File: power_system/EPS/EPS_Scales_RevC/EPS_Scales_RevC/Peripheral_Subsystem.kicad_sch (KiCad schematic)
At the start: 6 parts, among them J13 G125-MH11605L3P

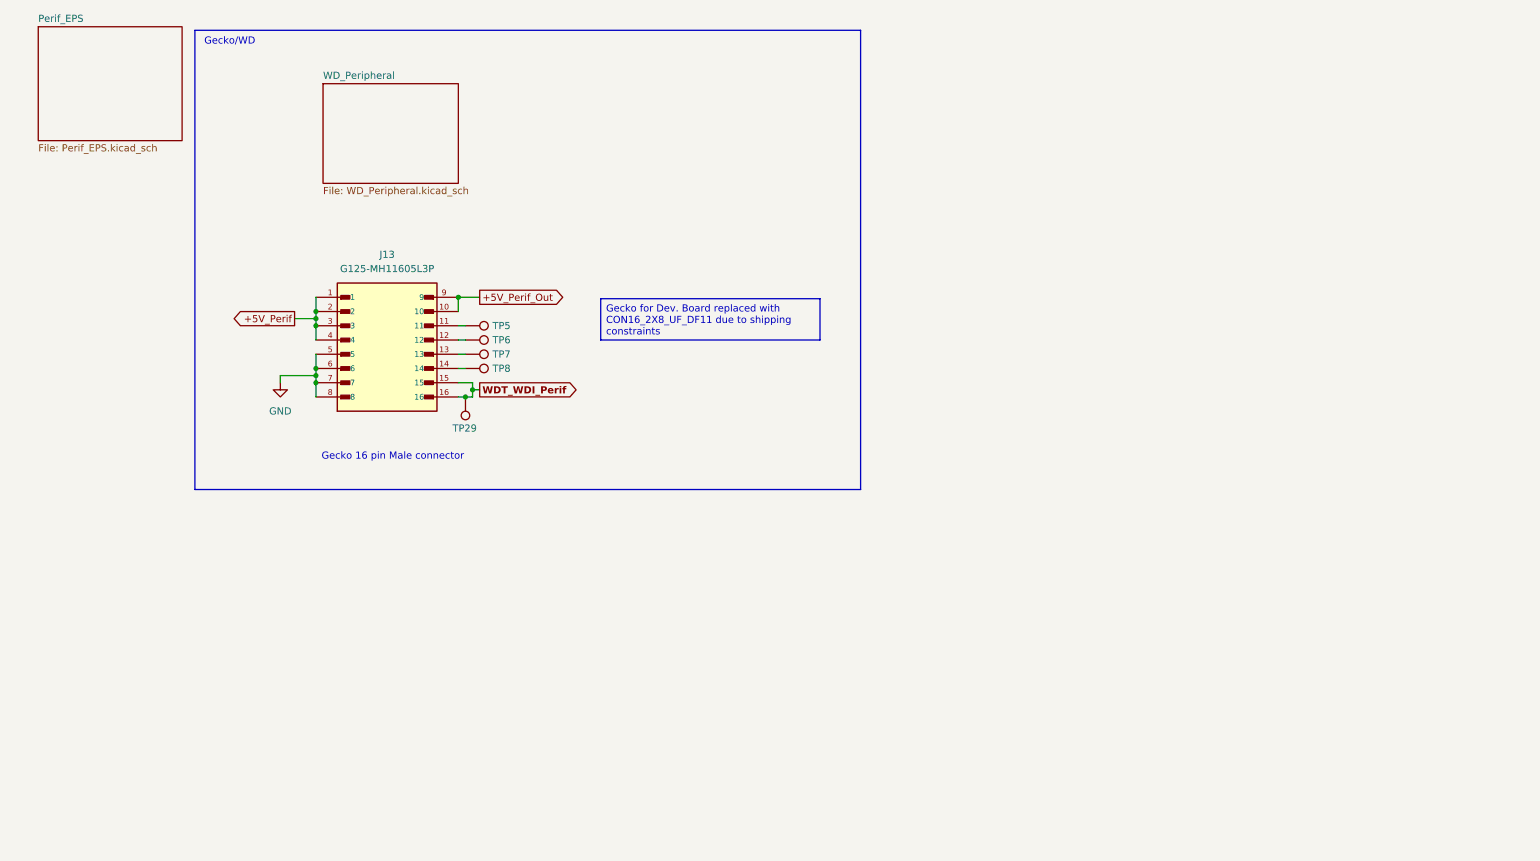
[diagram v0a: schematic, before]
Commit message: Rev C Schematic DONE
Components were finalized in meeting with Andrew Greenberg today, footprints have been assigned and specific component sizes and values have also been confirmed. Moving to layout for the first dev board of the SCALES EPS board.
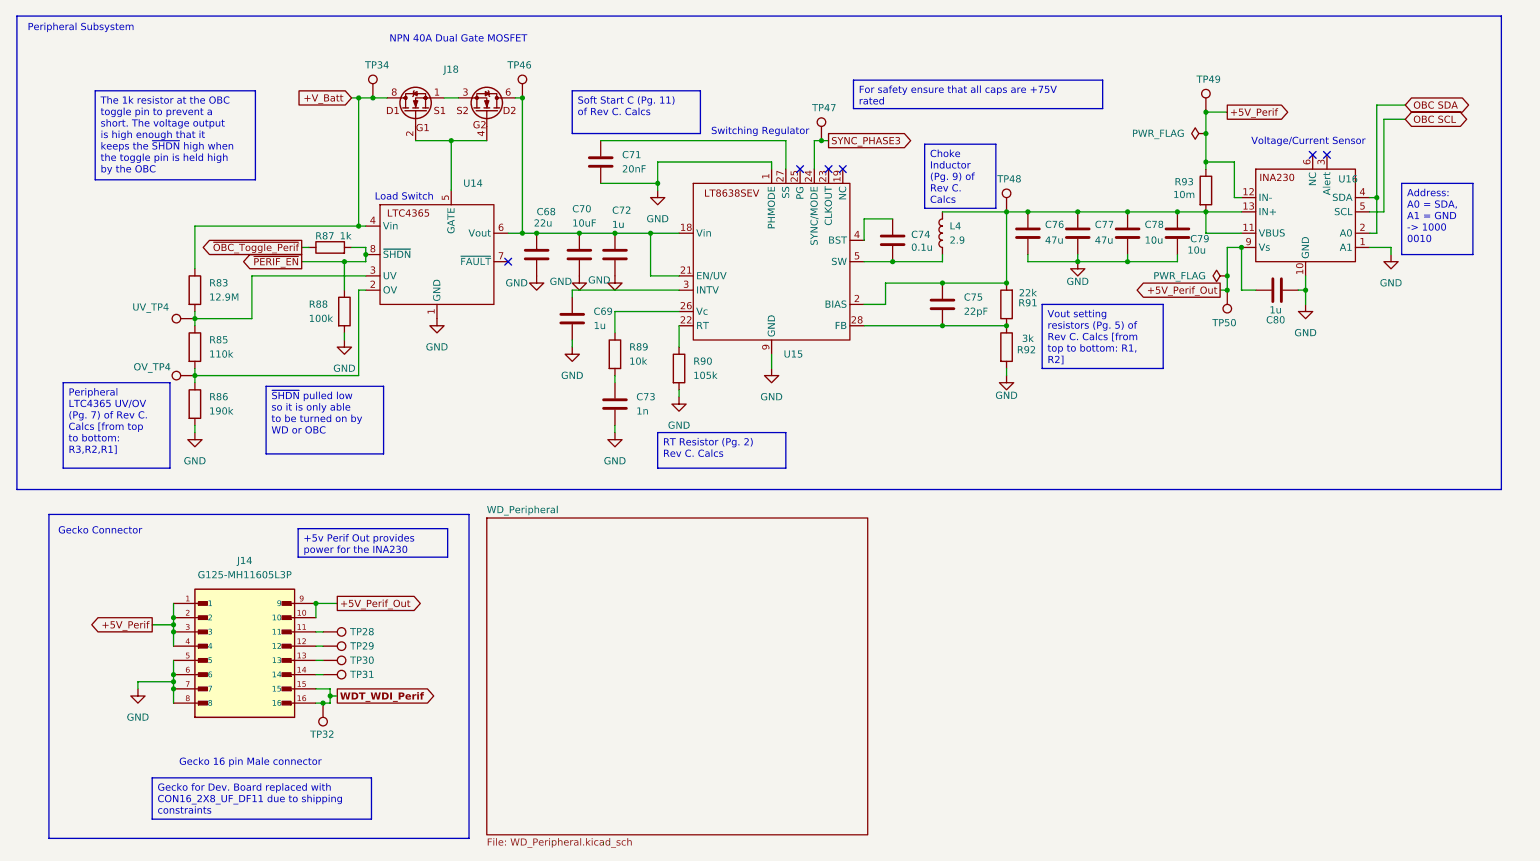
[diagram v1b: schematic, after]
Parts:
- added C68: 22u, Resistor_SMD:R_1210_3225Metric, symbol Device:C
- added C69, C72, C80: 1u, Resistor_SMD:R_1210_3225Metric, symbol Device:C
- added C70: 10uF, Resistor_SMD:R_1210_3225Metric, symbol Device:C
- added C71: 20nF, Resistor_SMD:R_1210_3225Metric, symbol Device:C
- added C73: 1n, Resistor_SMD:R_1210_3225Metric, symbol Device:C
- added C74: 0.1u, Resistor_SMD:R_1210_3225Metric, symbol Device:C
- added C75: 22pF, Resistor_SMD:R_1210_3225Metric, symbol Device:C
- added C76, C77: 47u, Resistor_SMD:R_1210_3225Metric, symbol Device:C
- added C78, C79: 10u, Resistor_SMD:R_1210_3225Metric, symbol Device:C
- added J18: ~, RevC Footprints:SISB46DN-T1-GE3, symbol SISB46DN:SISB46DN
- added L4: 2.9, RevC Footprints:XEL6030102MEC, symbol Device:L
- added OV_TP4, TP34, TP46, TP47, TP48, TP49, TP50, UV_TP4: TestPoint, TestPoint:TestPoint_Pad_1.0x1.0mm, symbol Connector:TestPoint
- added R83: 12.9M, Resistor_SMD:R_0603_1608Metric, symbol Device:R
- added R85: 110k, Resistor_SMD:R_0603_1608Metric, symbol Device:R
- added R86: 190k, Resistor_SMD:R_0603_1608Metric, symbol Device:R
- added R87: 1k, Resistor_SMD:R_0603_1608Metric, symbol Device:R
- added R88: 100k, Resistor_SMD:R_0603_1608Metric, symbol Device:R
- added R89: 10k, Resistor_SMD:R_0603_1608Metric, symbol Device:R
- added R90: 105k, Resistor_SMD:R_0603_1608Metric, symbol Device:R
- added R91: 22k, Resistor_SMD:R_0603_1608Metric, symbol Device:R
- added R92: 3k, Resistor_SMD:R_0603_1608Metric, symbol Device:R
- added R93: 10m, Resistor_SMD:R_2512_6332Metric, symbol Device:R
- added U14: ~, RevC Footprints:LTC4365, symbol LTC4365:LTC4365
- added U15: ~, RevC Footprints:LT8638SEVPBF, symbol LT8638SEV#PBF:LT863SEV#PBF
- added U16: INA230, RevC Footprints:INA230AIRGTT, symbol INA230:INA230 [RGT PACKAGE]
- renumbered J13 to J14, TP5 to TP28, TP6 to TP29, TP7 to TP30, TP8 to TP31, TP29 to TP32
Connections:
- net +5V_Perif: now also R93.1, TP49.1, U16.12 (IN-)
- net +5V_Perif_Out: now also C80.2, TP50.1, U16.9 (Vs)
- net GND: now also C68.2, C69.2, C70.2, C71.2, C72.2, C73.2, C76.2, C77.2, C78.2, C79.2, C80.1, R86.2, R88.2, R90.2, R92.2, U14.1 (GND), U15.1 (PHMODE), U15.9 (GND), U16.1 (A1), U16.10 (GND)
- new net: OV_TP4.1, R85.2, R86.1, U14.2 (OV)
- new net: J18.1, J18.3
- new net: J18.2, J18.4, U14.5 (GATE)
- new net: C68.1, C70.1, C72.1, J18.5, J18.6, TP46.1, U14.6 (Vout), U15.18 (Vin), U15.21 (EN/UV)
- new net: C75.1, C76.1, C77.1, C78.1, C79.1, L4.2, R91.2, R93.2, TP48.1, U15.2 (BIAS), U16.11 (VBUS), U16.13 (IN+)
- new net: C75.2, R91.1, R92.1, U15.28 (FB)
- new net: C71.1, U15.27 (SS)
- new net: R83.2, R85.1, U14.3 (UV), UV_TP4.1
- new net: C73.1, R89.2
- new net: R89.1, U15.26 (Vc)
- new net: C74.2, L4.1, U15.5 (SW)
- new net: R90.1, U15.22 (RT)
- new net: C69.1, U15.3 (INTV)
- new net: C74.1, U15.4 (BST)
- new net +V_Batt: J18.7, J18.8, R83.1, TP34.1, U14.4 (Vin)
- new net OBC SCL: U16.5 (SCL)
- new net OBC SDA: U16.2 (A0), U16.4 (SDA)
- new net SYNC_PHASE3: TP47.1, U15.24 (SYNC/MODE)
- new net ~{OBC_Toggle_Perif}: R87.1
- new net ~{PERIF_EN}: R87.2, R88.1, U14.8 (~{SHDN})
- no-connect marks 0 -> 6
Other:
- removed sheet Perif_EPS
- note added: "Gecko Connector"
- note added: "Load Switch"
- note added: "NPN 40A Dual Gate MOSFET"
- note added: "Peripheral Subsystem"
- note added: "Switching Regulator"
- note added: "Voltage/Current Sensor"
- note removed: "Gecko/WD"
- moved on the sheet: J14, TP28, TP29, TP30, TP31, TP32

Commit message: Rev C Layout #2 electric boogaloo
Yes
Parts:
- added L7, L8: 1u, RevC Footprints:XEL6030102MEC, symbol Device:L
- C68, C69, C72, C73, C74, C76, C77, C78, C79, C80: footprint Resistor_SMD:R_1210_3225Metric -> Capacitor_SMD:C_1210_3225Metric
- C70: value 10uF -> 10u; footprint Resistor_SMD:R_1210_3225Metric -> Capacitor_SMD:C_1210_3225Metric
- C71: value 20nF -> 20n; footprint Resistor_SMD:R_1210_3225Metric -> Capacitor_SMD:C_1210_3225Metric
- C75: value 22pF -> 22p; footprint Resistor_SMD:R_1210_3225Metric -> Capacitor_SMD:C_1210_3225Metric
- L4: value 2.9 -> 1u
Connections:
- net at C75.1, C76.1, C77.1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: now also L8.2; no longer L4.2
- new net: L4.2, L7.1
- new net: L7.2, L8.1
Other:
- moved on the sheet: TP48
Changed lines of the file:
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@@
 	(text_box "For safety ensure that all caps are +75V rated"
 		(exclude_from_sim no)
-		(at 165.735 26.035 0)
+		(at 163.83 27.305 0)
 		(size 44.45 5.08)
 		(margins 0.9525 0.9525 0.9525 0.9525)
@@
 		)
 	)
+	(text_box "No 3u available so 3*1u inductors"
+		(exclude_from_sim no)
+		(at 195.58 34.925 0)
+		(size 19.05 8.255)
+		(margins 0.9525 0.9525 0.9525 0.9525)
+		(stroke
+			(width 0)
+			(type solid)
+		)
+		(fill
+			(type none)
+		)
+		(effects
+			(font
+				(size 1.27 1.27)
+			)
+			(justify left top)
+		)
+	)
 	(text_box "Peripheral LTC4365 UV/OV (Pg. 7) of Rev C. Calcs [from top to bottom: R3,R2,R1]"
 		(exclude_from_sim no)
@@
 	(text_box "Choke Inductor (Pg. 9) of Rev C. Calcs"
 		(exclude_from_sim no)
-		(at 178.435 37.465 0)
+		(at 169.545 14.605 0)
 		(size 12.7 11.43)
 		(margins 0.9525 0.9525 0.9525 0.9525)
@@
 	)
 	(junction
+		(at 193.04 45.72)
+		(diameter 0)
+		(color 0 0 0 0)
+	)
+	(junction
 		(at 196.85 49.53)
 		(diameter 0)
@@
 	(wire
 		(pts
+			(xy 193.04 34.29) (xy 193.04 45.72)
+		)
+		(stroke
+			(width 0)
+			(type default)
+		)
+	)
+	(wire
+		(pts
 			(xy 38.1 134.62) (xy 38.1 133.35)
 		)
@@
 	(wire
 		(pts
+			(xy 193.04 45.72) (xy 193.04 49.53)
+		)
+		(stroke
+			(width 0)
+			(type default)
+		)
+	)
+	(wire
+		(pts
 			(xy 167.64 58.42) (xy 172.72 58.42)
 		)
@@
 	(wire
 		(pts
-			(xy 193.04 49.53) (xy 181.61 49.53)
-		)
-		(stroke
-			(width 0)
-			(type default)
-		)
-	)
-	(wire
-		(pts
 			(xy 67.31 58.42) (xy 74.93 58.42)
 		)
@@
 	(wire
 		(pts
+			(xy 181.61 34.29) (xy 193.04 34.29)
+		)
+		(stroke
+			(width 0)
+			(type default)
+		)
+	)
+	(wire
+		(pts
 			(xy 223.52 49.53) (xy 228.6 49.53)
 		)
@@
 			)
 		)
-		(property "Value" "22pF"
+		(property "Value" "22p"
 			(at 185.42 67.3099 0)
 			(effects
@@
 			)
 		)
-		(property "Footprint" "Resistor_SMD:R_1210_3225Metric"
+		(property "Footprint" "Capacitor_SMD:C_1210_3225Metric"
 			(at 182.5752 69.85 0)
 			(effects
@@
 			)
 		)
-		(property "Footprint" "Resistor_SMD:R_1210_3225Metric"
+		(property "Footprint" "Capacitor_SMD:C_1210_3225Metric"
 			(at 237.49 64.4652 0)
 			(effects
@@
 			)
 		)
-		(property "Value" "10uF"
+		(property "Value" "10u"
 			(at 115.57 51.562 0)
 			(effects
@@
 			)
 		)
-		(property "Footprint" "Resistor_SMD:R_1210_3225Metric"
+		(property "Footprint" "Capacitor_SMD:C_1210_3225Metric"
 			(at 117.8052 60.96 0)
 			(effects
@@
 			)
 		)
-		(property "Value" "20nF"
+		(property "Value" "20n"
 			(at 124.46 41.9099 0)
 			(effects
@@
 			)
 		)
-		(property "Footprint" "Resistor_SMD:R_1210_3225Metric"
+		(property "Footprint" "Capacitor_SMD:C_1210_3225Metric"
 			(at 121.6152 44.45 0)
 			(effects
@@
 	)
 	(symbol
+		(lib_id "Device:L")
+		(at 181.61 45.72 180)
+		(unit 1)
+		(exclude_from_sim no)
+		(in_bom yes)
+		(on_board yes)
+		(dnp no)
+		(fields_autoplaced yes)
+		(property "Reference" "L7"
+			(at 182.88 44.4499 0)
+			(effects
+				(font
+					(size 1.27 1.27)
+				)
+				(justify right)
+			)
+		)
+		(property "Value" "1u"
+			(at 182.88 46.9899 0)
+			(effects
+				(font
+					(size 1.27 1.27)
+				)
+				(justify right)
+			)
+		)
+		(property "Footprint" "RevC Footprints:XEL6030102MEC"
+			(at 181.61 45.72 0)
+			(effects
+				(font
+					(size 1.27 1.27)
+				)
+				(hide yes)
+			)
+		)
+		(property "Datasheet" "https://www.coilcraft.com/en-us/products/power/shielded-inductors/molded-inductor/xel/xel6030/?srsltid=AfmBOoqxe6hS-AVIr3woqGFRZjt3QaXyQi86MwGE0zvqKz2AENsjz4RA"
+			(at 181.61 45.72 0)
+			(effects
+				(font
+					(size 1.27 1.27)
+				)
+				(hide yes)
+			)
+		)
+		(property "Description" "Coilcraft XEL6030-102 Power Inductor"
+			(at 181.61 45.72 0)
+			(effects
+				(font
+					(size 1.27 1.27)
+				)
+				(hide yes)
+			)
+		)
+		(pin "2"
+		)
+		(pin "1"
+		)
+		(instances
+			(project "EPS_Scales_RevC"
+				(path "/f3bdc9b1-4369-4cfa-b765-d952bf408a7b/9f608de4-3574-4917-924e-b2449769bafa"
+					(reference "L7")
+					(unit 1)
+				)
+			)
+		)
+	)
+	(symbol
 		(lib_id "LTC4365:LTC4365")
 		(at 92.71 57.15 0)
@@
 	(symbol
 		(lib_id "Connector:TestPoint")
-		(at 193.04 49.53 0)
+		(at 193.04 45.72 270)
 		(unit 1)
 		(exclude_from_sim no)
@@
 		(dnp no)
 		(property "Reference" "TP48"
-			(at 193.548 43.688 0)
+			(at 198.882 46.228 0)
 			(effects
 				(font
@@
 		)
 		(property "Value" "TestPoint"
-			(at 195.58 46.228 90)
+			(at 196.342 48.26 90)
 			(effects
 				(font
@@
 		)
 		(property "Footprint" "TestPoint:TestPoint_Pad_1.0x1.0mm"
-			(at 198.12 49.53 0)
+			(at 193.04 50.8 0)
 			(effects
 				(font
@@
 		)
 		(property "Datasheet" "~"
-			(at 198.12 49.53 0)
+			(at 193.04 50.8 0)
 			(effects
 				(font
@@
 		)
 		(property "Description" "test point"
-			(at 193.04 49.53 0)
+			(at 193.04 45.72 0)
 			(effects
 				(font
@@
 			)
 		)
-		(property "Footprint" "Resistor_SMD:R_1210_3225Metric"
+		(property "Footprint" "Capacitor_SMD:C_1210_3225Metric"
 			(at 124.1552 87.63 0)
 			(effects
@@
 			)
 		)
-		(property "Value" "2.9"
+		(property "Value" "1u"
 			(at 182.88 54.6099 0)
 			(effects
@@
 	)
 	(symbol
+		(lib_id "Device:L")
+		(at 181.61 38.1 180)
+		(unit 1)
+		(exclude_from_sim no)
+		(in_bom yes)
+		(on_board yes)
+		(dnp no)
+		(fields_autoplaced yes)
+		(property "Reference" "L8"
+			(at 182.88 36.8299 0)
+			(effects
+				(font
+					(size 1.27 1.27)
+				)
+				(justify right)
+			)
+		)
+		(property "Value" "1u"
+			(at 182.88 39.3699 0)
+			(effects
+				(font
+					(size 1.27 1.27)
+				)
+				(justify right)
+			)
+		)
+		(property "Footprint" "RevC Footprints:XEL6030102MEC"
+			(at 181.61 38.1 0)
+			(effects
+				(font
+					(size 1.27 1.27)
+				)
+				(hide yes)
+			)
+		)
+		(property "Datasheet" "https://www.coilcraft.com/en-us/products/power/shielded-inductors/molded-inductor/xel/xel6030/?srsltid=AfmBOoqxe6hS-AVIr3woqGFRZjt3QaXyQi86MwGE0zvqKz2AENsjz4RA"
+			(at 181.61 38.1 0)
+			(effects
+				(font
+					(size 1.27 1.27)
+				)
+				(hide yes)
+			)
+		)
+		(property "Description" "Coilcraft XEL6030-102 Power Inductor"
+			(at 181.61 38.1 0)
+			(effects
+				(font
+					(size 1.27 1.27)
+				)
+				(hide yes)
+			)
+		)
+		(pin "2"
+		)
+		(pin "1"
+		)
+		(instances
+			(project "EPS_Scales_RevC"
+				(path "/f3bdc9b1-4369-4cfa-b765-d952bf408a7b/9f608de4-3574-4917-924e-b2449769bafa"
+					(reference "L8")
+					(unit 1)
+				)
+			)
+		)
+	)
+	(symbol
 		(lib_id "Device:C")
 		(at 223.52 53.34 0)
@@
 			)
 		)
-		(property "Footprint" "Resistor_SMD:R_1210_3225Metric"
+		(property "Footprint" "Capacitor_SMD:C_1210_3225Metric"
 			(at 224.4852 57.15 0)
 			(effects
@@
 			)
 		)
-		(property "Footprint" "Resistor_SMD:R_1210_3225Metric"
+		(property "Footprint" "Capacitor_SMD:C_1210_3225Metric"
 			(at 124.1552 60.96 0)
 			(effects
@@
 			)
 		)
-		(property "Footprint" "Resistor_SMD:R_1210_3225Metric"
+		(property "Footprint" "Capacitor_SMD:C_1210_3225Metric"
 			(at 215.5952 57.15 0)
 			(effects
@@
 			)
 		)
-		(property "Footprint" "Resistor_SMD:R_1210_3225Metric"
+		(property "Footprint" "Capacitor_SMD:C_1210_3225Metric"
 			(at 197.8152 57.15 0)
 			(effects
@@
 			)
 		)
-		(property "Footprint" "Resistor_SMD:R_1210_3225Metric"
+		(property "Footprint" "Capacitor_SMD:C_1210_3225Metric"
 			(at 110.1852 60.96 0)
 			(effects
@@
 			)
 		)
-		(property "Footprint" "Resistor_SMD:R_1210_3225Metric"
+		(property "Footprint" "Capacitor_SMD:C_1210_3225Metric"
 			(at 173.6852 58.42 0)
 			(effects
@@
 			)
 		)
-		(property "Footprint" "Resistor_SMD:R_1210_3225Metric"
+		(property "Footprint" "Capacitor_SMD:C_1210_3225Metric"
 			(at 206.7052 57.15 0)
 			(effects
@@
 			)
 		)
-		(property "Footprint" "Resistor_SMD:R_1210_3225Metric"
+		(property "Footprint" "Capacitor_SMD:C_1210_3225Metric"
 			(at 116.5352 72.39 0)
 			(effects
